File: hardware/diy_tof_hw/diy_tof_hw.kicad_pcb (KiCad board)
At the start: 4 copper layers, 90 x 100 mm, 83 parts, among them IC1 TDC7200PWR, IC2 TDC7200PWR, IC21 74LVC1G08QW5-7, IC22 LMG1025QDEETQ1, J1 Conn_01x02_Pin, J2 Conn_01x03_Pin, J3 Conn_01x02_Pin, SW1 SW_Nidec_CAS-120A1, SW2 SW_Nidec_CAS-120A1, U1 NUCLEO-F042K6, U2 OPA858xDSG, U3 TLV3501AIDBV, X1 SG-5032CAN

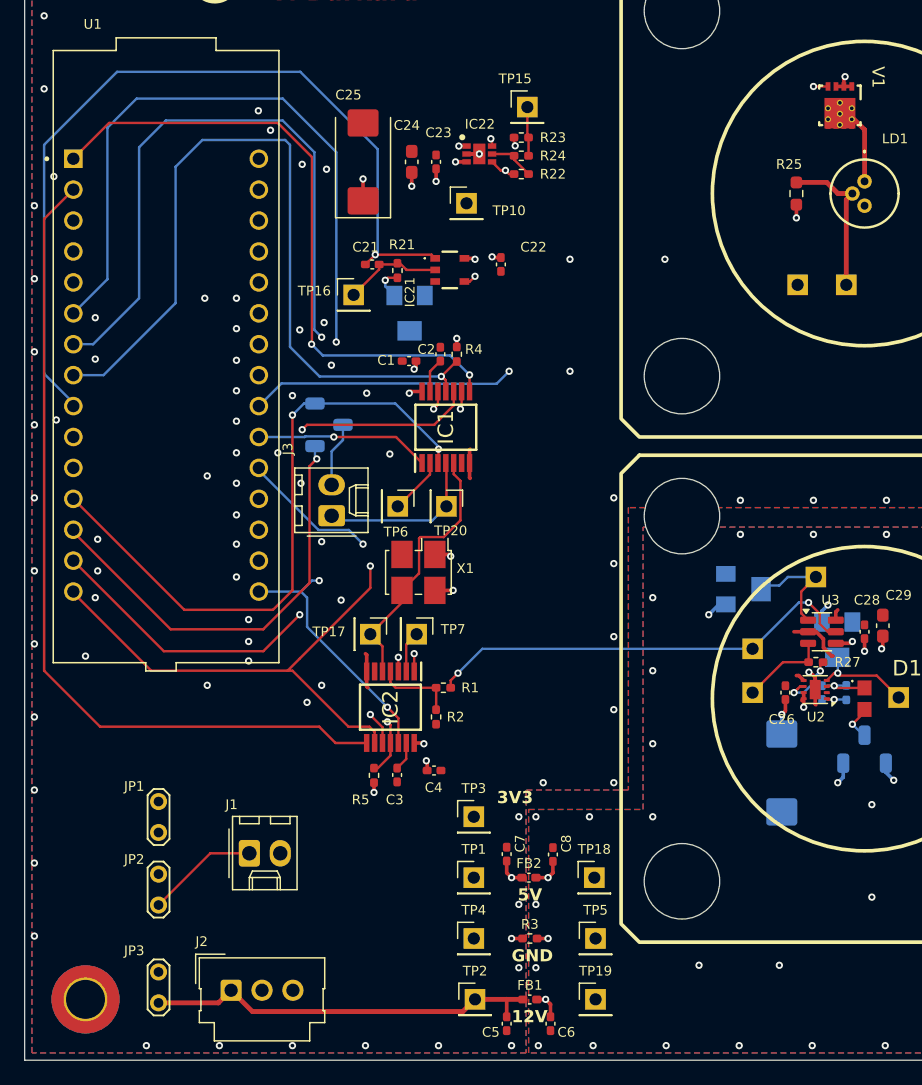
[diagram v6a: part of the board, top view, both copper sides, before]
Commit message: [hardware] enlarged planes so that the PCB won't be produced with asymmetric copper planes  - also added gerber output job
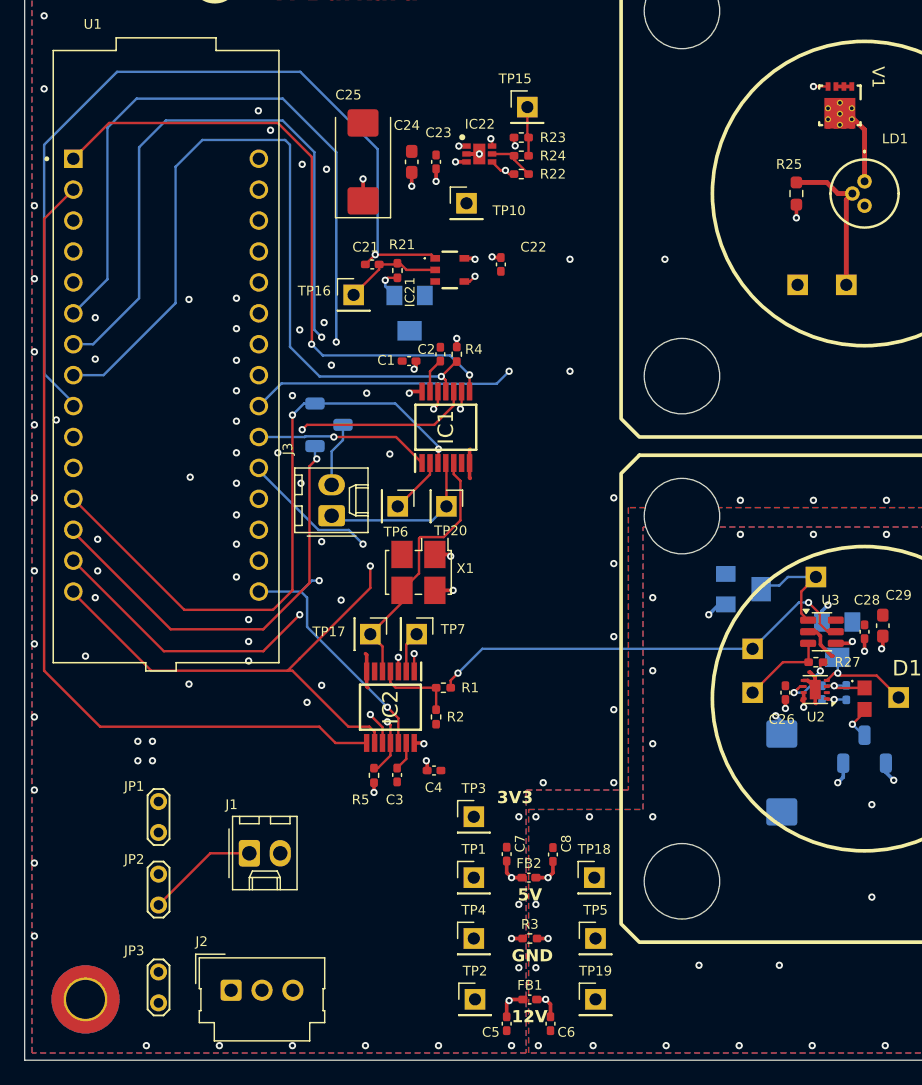
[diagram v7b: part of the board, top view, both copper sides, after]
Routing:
- net /Power_Nucleo_TDC/12_nuc: track 72.5 -> 0.00 mm, vias 0 -> 4
- net 5V_nuc: track 48.6 -> 0.00 mm
- net 12V: track 32.9 -> 2.58 mm, vias 0 -> 1
- net GNDA: track 10.4 -> 8.82 mm, vias 33 -> 32
- net GND: track 10.8 -> 9.93 mm, vias 100 -> 98
- net 5V_LN: track 15.7 -> 15.1 mm, vias 9 -> 10
- added copper zone on In1.Cu, net /Power_Nucleo_TDC/12_nuc
- added copper zone on In2.Cu, net /Power_Nucleo_TDC/12_nuc
- added copper zone on In1.Cu, net 12V
- added copper zone on In1.Cu, net 5V_ext
- added copper zone on In1.Cu, net 5V_nuc

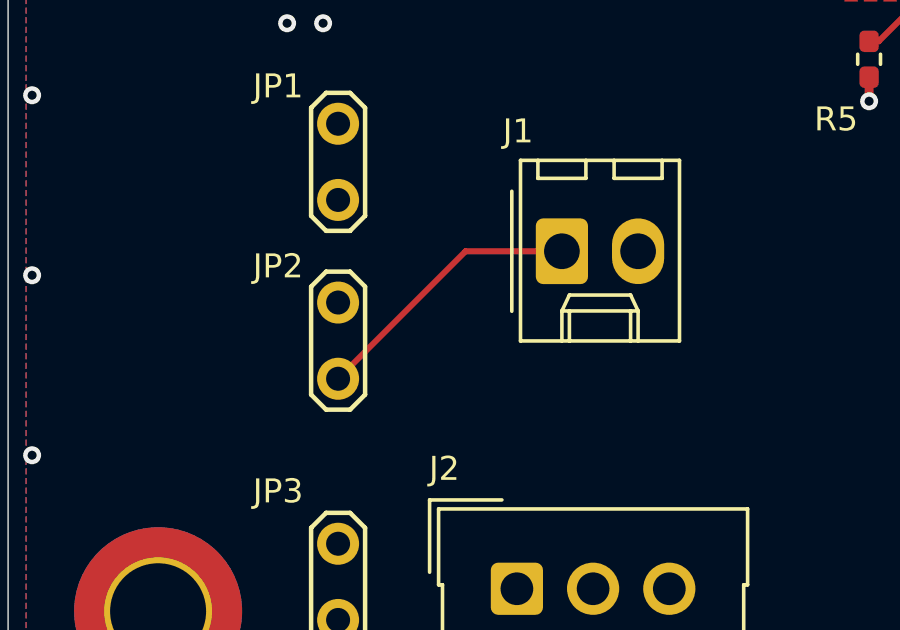
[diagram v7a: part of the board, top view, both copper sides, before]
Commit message: [hardware] minor plane adjustments, removed a connection which is done via plane
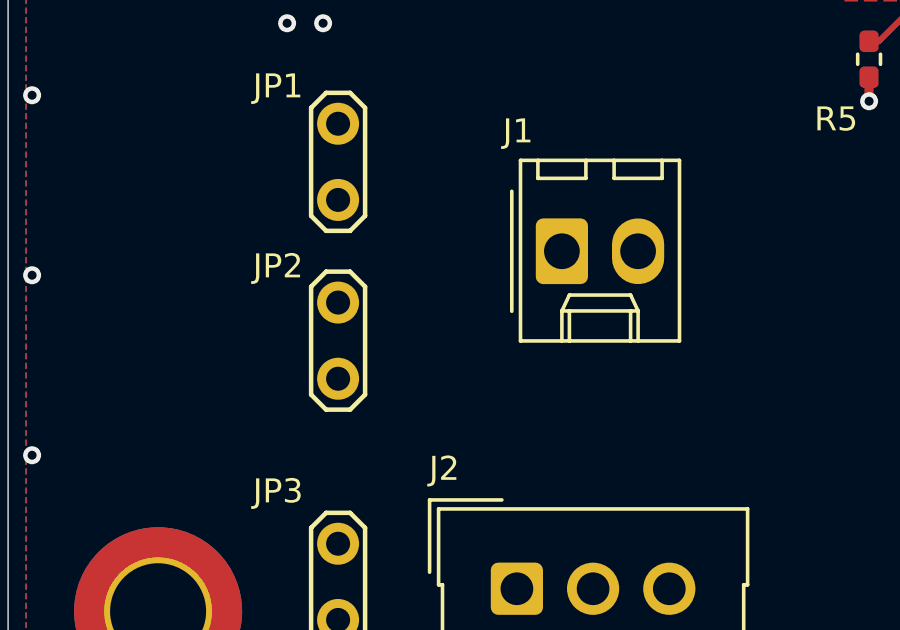
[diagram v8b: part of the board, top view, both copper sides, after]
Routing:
- net 5V_ext: track 9.22 -> 0.00 mm
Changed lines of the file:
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@@
 	)
 	(segment
-		(start 61.25 113)
-		(end 57 117.25)
-		(width 0.2)
-		(layer "F.Cu")
-		(net 5)
-	)
-	(segment
-		(start 64.46 113)
-		(end 61.25 113)
-		(width 0.2)
-		(layer "F.Cu")
-		(net 5)
-	)
-	(segment
 		(start 79.423669 63.823669)
 		(end 79.725 64.125)
@@
 		(polygon
 			(pts
-				(xy 46.6 129.4) (xy 46.6 30.6) (xy 135.4 30.6) (xy 135.4 84.6) (xy 125.4 84.6) (xy 125.4 84.6) (xy 95.6 84.6)
-				(xy 95.6 107.8) (xy 87.2 107.8) (xy 87.2 129.4)
+				(xy 46.6 129.4) (xy 46.6 30.6) (xy 135.4 30.6) (xy 135.4 84.6) (xy 125.4 84.6) (xy 95.6 84.6) (xy 95.6 107.8)
+				(xy 87.2 107.8) (xy 87.2 129.4)
 			)
 		)
@@
 		(polygon
 			(pts
-				(xy 65.2 87.6) (xy 65.2 90.2) (xy 69.4 90.2) (xy 69.4 111.6) (xy 86.6 111.6) (xy 86.6 62.8) (xy 69.4 62.8)
-				(xy 69.4 87.6)
+				(xy 65.2 87.8) (xy 65.2 90.1) (xy 69.4 91) (xy 69.4 111.6) (xy 86.6 111.6) (xy 86.6 62.8) (xy 69.4 62.8)
+				(xy 69.3 86.6)
 			)
 		)
